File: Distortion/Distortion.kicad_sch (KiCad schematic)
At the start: 36 parts, among them J1 Input, J2 Output, Q1 2N3819, U1 OP07

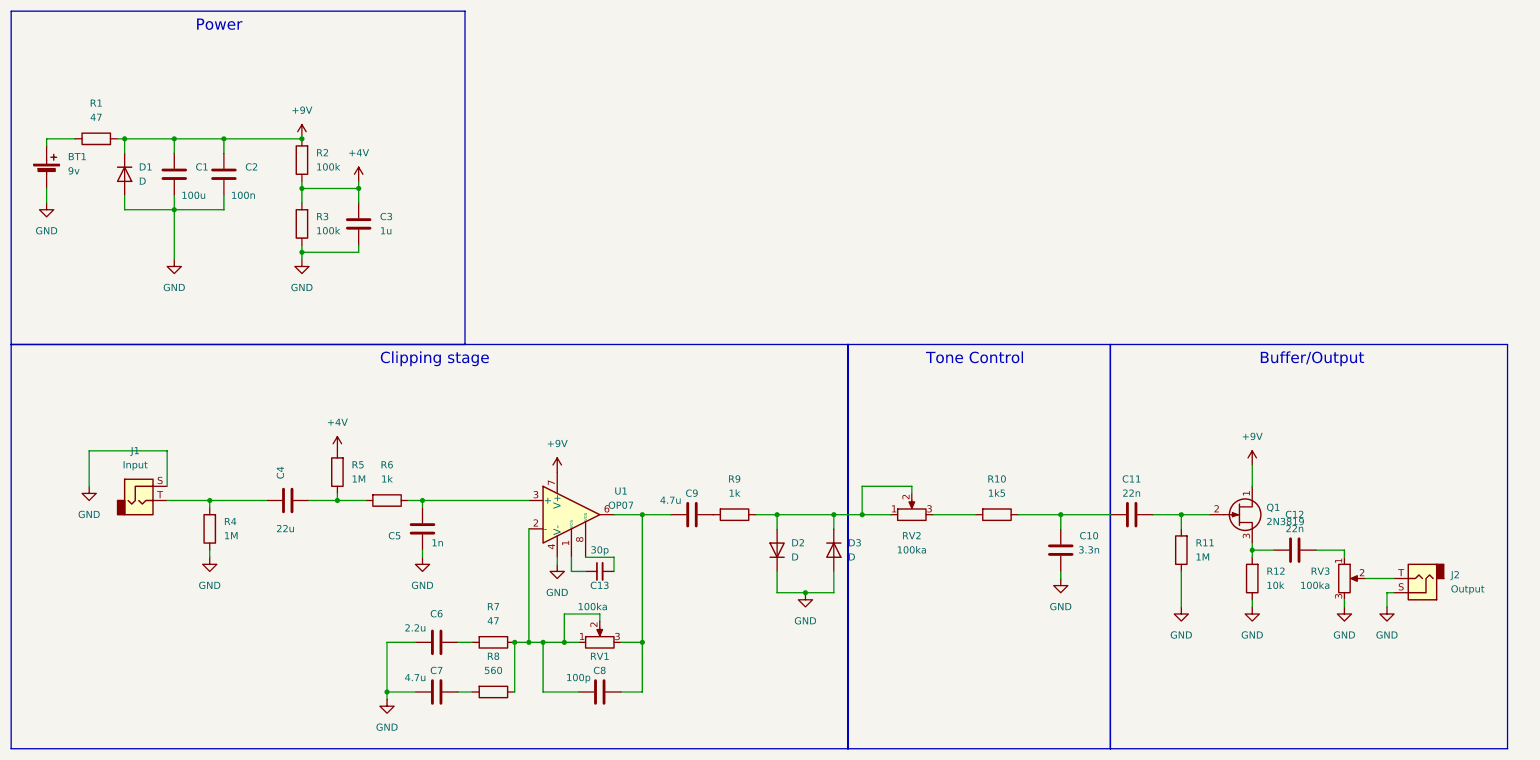
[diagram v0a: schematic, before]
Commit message: finished distortion pcb but kinda want to rethink how to approach this pcb
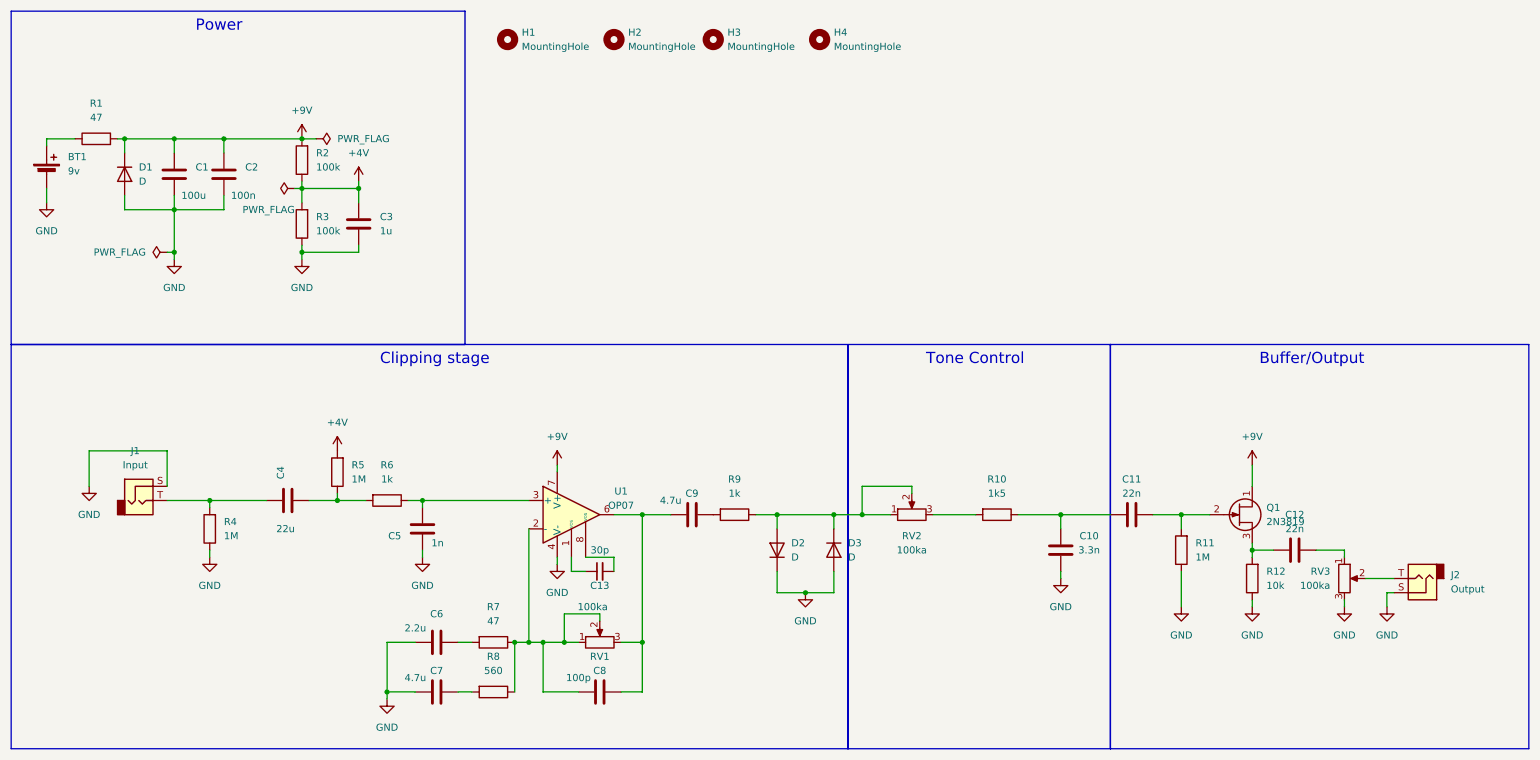
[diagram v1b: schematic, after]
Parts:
- added H1, H2, H3, H4: MountingHole, MountingHole:MountingHole_3.5mm_Pad_Via, symbol Mechanical:MountingHole
- C1, C10, C11, C12, C13, C2, C3, C4, C5, C6, C7, C8, C9: footprint (none) -> Capacitor_THT:C_Disc_D10.5mm_W5.0mm_P10.00mm
- D1, D2, D3: footprint (none) -> Diode_THT:D_DO-15_P12.70mm_Horizontal
- J1, J2: footprint (none) -> Connector_Audio:Jack_6.35mm_Neutrik_NMJ4HHD2_Horizontal
- R1, R10, R11, R12, R2, R3, R4, R5, R6, R7, R8, R9: footprint (none) -> Resistor_THT:R_Axial_DIN0207_L6.3mm_D2.5mm_P10.16mm_Horizontal
- RV1, RV2, RV3: footprint (none) -> Potentiometer_THT:Potentiometer_Alps_RK09K_Single_Vertical
- U1: footprint (none) -> Package_DIP:DIP-8_W7.62mm_LongPads
